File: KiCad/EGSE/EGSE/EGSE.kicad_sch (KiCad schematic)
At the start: 0 parts

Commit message: Kicad is my hell
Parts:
- added MOSFET1, MOSFET2: SIS412DN-T1-GE3, POWERPAK_1212-8, symbol 2025-09-18_19-47-42:SIS412DN-T1-GE3
- added MOSFET3, MOSFET4: SI7617DN-T1-GE3, POWERPAK_1212-8_VIS, symbol 2025-09-18_19-46-24:SI7617DN-T1-GE3
- added U1: BQ24610, Package_DFN_QFN:VQFN-24-1EP_4x4mm_P0.5mm_EP2.45x2.45mm, symbol Battery_Management:BQ24610
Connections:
- new net: MOSFET3.1 (S), MOSFET3.2 (S), MOSFET3.3 (S)
- new net: MOSFET3.5 (D), MOSFET3.6 (D), MOSFET3.7 (D), MOSFET3.8 (D)
- new net: MOSFET1.1 (S), MOSFET1.2 (S), MOSFET1.3 (S), MOSFET2.5 (D), MOSFET2.6 (D), MOSFET2.7 (D), MOSFET2.8 (D), U1.20 (PH)
- new net: MOSFET1.4 (G), U1.21 (HIDRV)
- new net: MOSFET1.5 (D), MOSFET1.6 (D), MOSFET1.7 (D), MOSFET1.8 (D)
- new net: MOSFET2.4 (G), U1.19 (LODRV)
- new net: MOSFET4.1 (S), MOSFET4.2 (S), MOSFET4.3 (S)
- new net: MOSFET4.5 (D), MOSFET4.6 (D), MOSFET4.7 (D), MOSFET4.8 (D)
- new net GND: MOSFET2.1 (S), MOSFET2.2 (S), MOSFET2.3 (S), U1.17 (GND), U1.25 (GND)

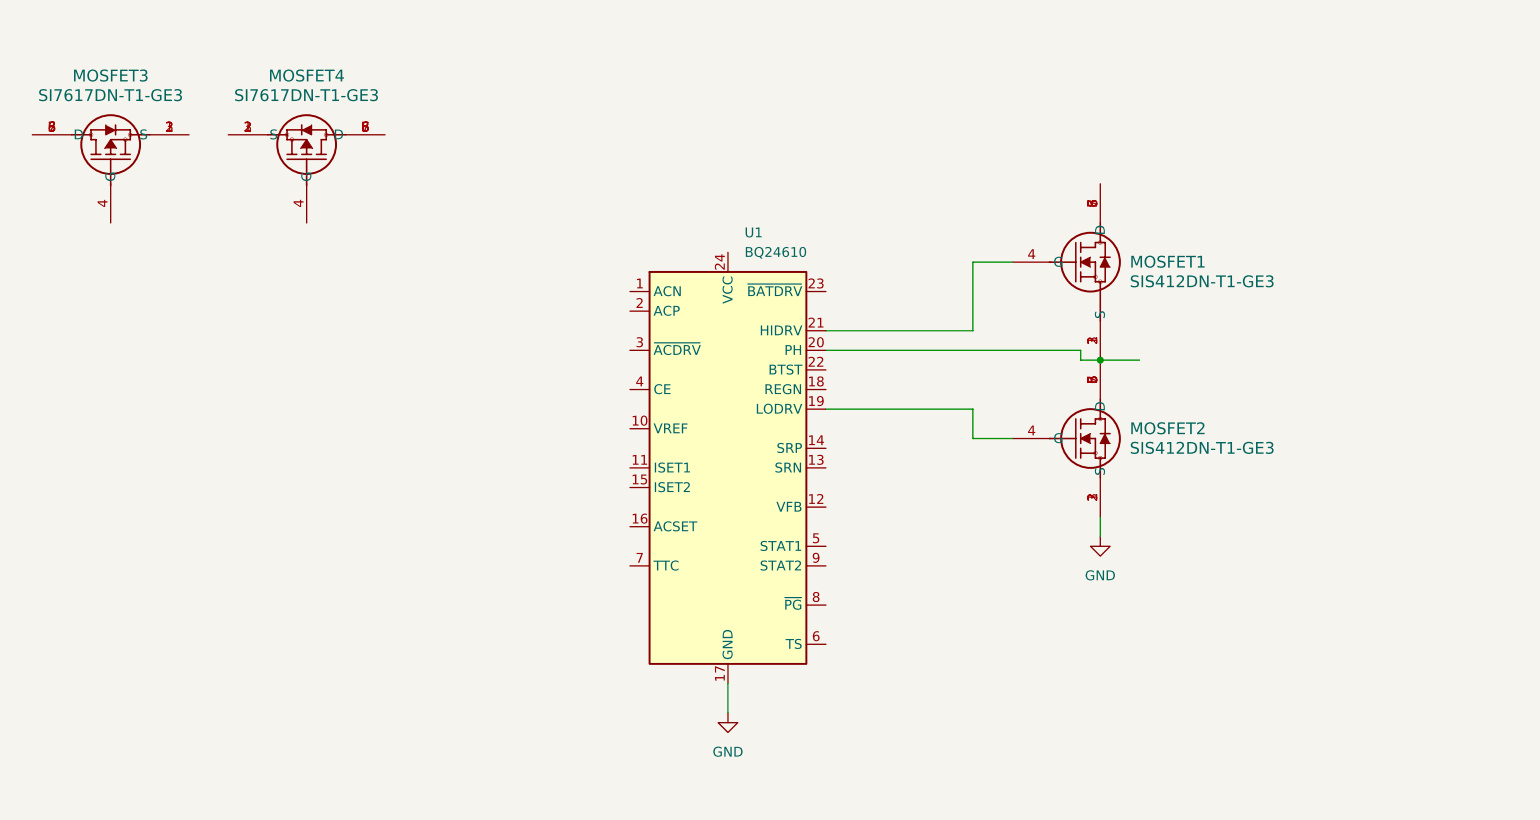
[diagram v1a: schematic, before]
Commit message: Battery Charge Schematic Done
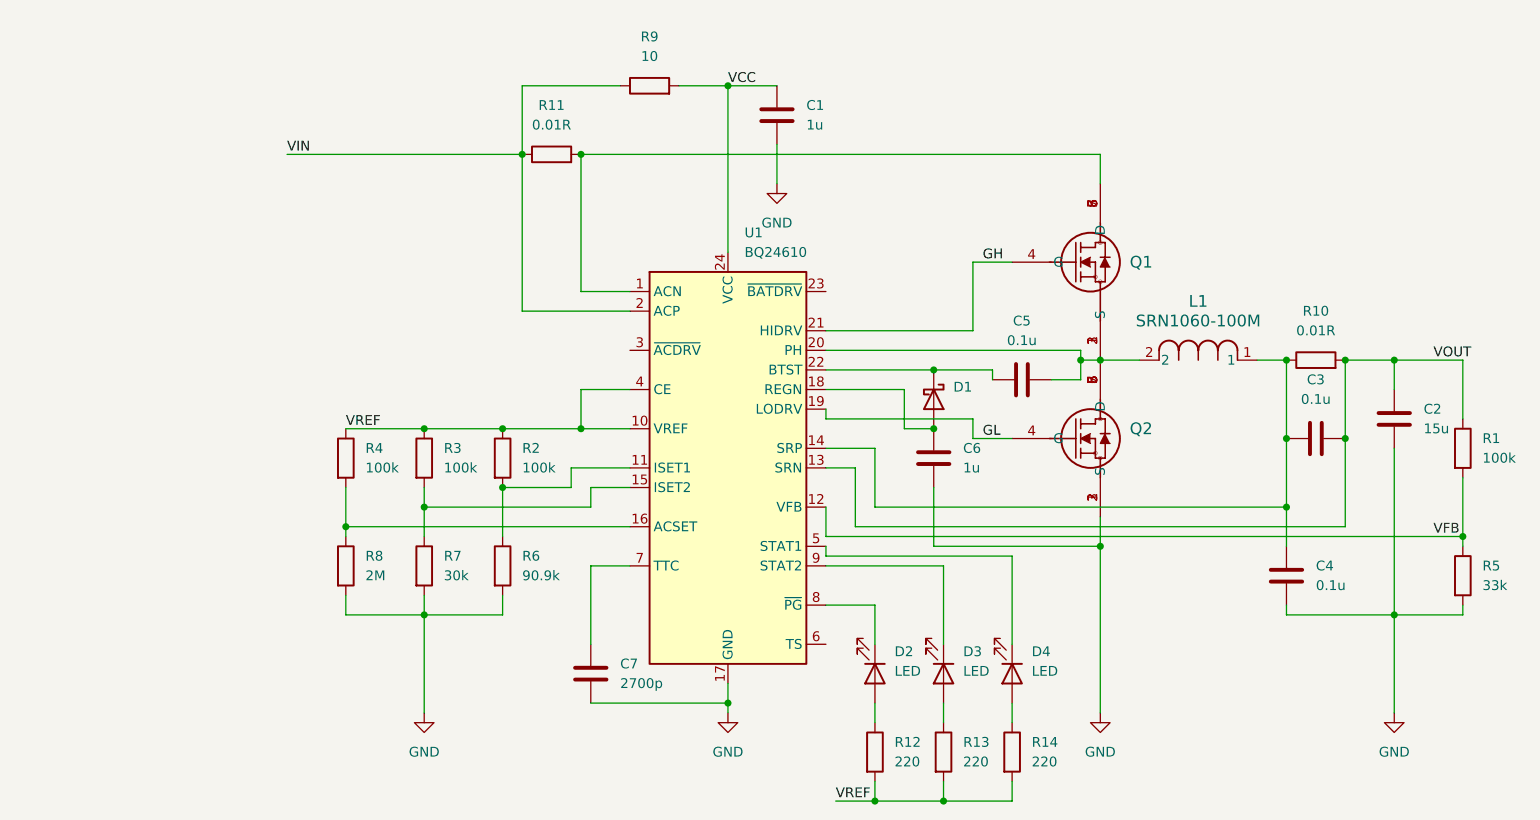
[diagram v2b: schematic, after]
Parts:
- removed MOSFET3, MOSFET4: SI7617DN-T1-GE3, POWERPAK_1212-8_VIS, symbol 2025-09-18_19-46-24:SI7617DN-T1-GE3
- added C1, C6: 1u, Capacitor_SMD:C_0805_2012Metric, symbol Device:C
- added C2: 15u, Capacitor_SMD:C_0805_2012Metric, symbol Device:C
- added C3, C4, C5: 0.1u, Capacitor_SMD:C_0805_2012Metric, symbol Device:C
- added C7: 2700p, Capacitor_SMD:C_0805_2012Metric, symbol Device:C
- added D1: D_Schottky, Diode_SMD:D_SOD-123, symbol Device:D_Schottky
- added D2, D3, D4: LED, symbol Device:LED
- added L1: SRN1060-100M, IND_BOURNS_SRN1060, symbol SRN1060-100M:SRN1060-100M
- added R1, R2, R3, R4: 100k, Resistor_SMD:R_0805_2012Metric, symbol Device:R
- added R10, R11: 0.01R, Resistor_SMD:R_0805_2012Metric, symbol Device:R
- added R12, R13, R14: 220, Resistor_SMD:R_0805_2012Metric, symbol Device:R
- added R5: 33k, Resistor_SMD:R_0805_2012Metric, symbol Device:R
- added R6: 90.9k, Resistor_SMD:R_0805_2012Metric, symbol Device:R
- added R7: 30k, Resistor_SMD:R_0805_2012Metric, symbol Device:R
- added R8: 2M, Resistor_SMD:R_0805_2012Metric, symbol Device:R
- added R9: 10, Resistor_SMD:R_0805_2012Metric, symbol Device:R
- renumbered MOSFET1 to Q1, MOSFET2 to Q2
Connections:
- net GND: now also C1.2, C2.2, C4.1, C6.2, C7.2, R5.2, R6.2, R7.2, R8.2
- net at Q1.1 (S), Q1.2 (S), Q1.3 (S)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: now also C5.2, L1.2
- net GH: now reaches Q1.4 (G), U1.21 (HIDRV)
- net at Q1.5 (D), Q1.6 (D), Q1.7 (D)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: now also U1.1 (ACN), R11.2
- net VREF: now reaches U1.10 (VREF)
- net VREF: now also U1.4 (CE), R12.2, R13.2, R14.2, R2.1, R3.1, R4.1
- net at U1.11 (ISET1): now also R2.2, R6.1
- net VFB: now reaches U1.12 (VFB)
- net VFB: now also R1.2, R5.1
- net VOUT: now reaches U1.13 (SRN)
- net VOUT: now also C2.1, C3.2, R1.1, R10.2
- net at U1.14 (SRP): now also C3.1, C4.2, L1.1, R10.1
- net at U1.15 (ISET2): now also R3.2, R7.1
- net at U1.16 (ACSET): now also R4.2, R8.1
- net at U1.18 (REGN): now also C6.1, D1.2 (A)
- net GL: now reaches Q2.4 (G), U1.19 (LODRV)
- net VIN: now reaches U1.2 (ACP)
- net VIN: now also R11.1, R9.1
- net at U1.22 (BTST): now also C5.1, D1.1 (K)
- net VCC: now reaches U1.24 (VCC)
- net VCC: now also C1.1, R9.2
- net at U1.5 (STAT1): now also D4.1 (K)
- net at U1.7 (TTC): now also C7.1
- net at U1.8 (~{PG}): now also D2.1 (K)
- net at U1.9 (STAT2): now also D3.1 (K)
- new net: D4.2 (A), R14.1
- new net: D3.2 (A), R13.1
- new net: D2.2 (A), R12.1

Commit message: Okay KICAD isn't so bad
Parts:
- removed C1, C6: 1u, Capacitor_SMD:C_0805_2012Metric, symbol Device:C
- removed C2: 15u, Capacitor_SMD:C_0805_2012Metric, symbol Device:C
- removed C3, C4, C5: 0.1u, Capacitor_SMD:C_0805_2012Metric, symbol Device:C
- removed C7: 2700p, Capacitor_SMD:C_0805_2012Metric, symbol Device:C
- removed D1: D_Schottky, Diode_SMD:D_SOD-123, symbol Device:D_Schottky
- removed D2, D3, D4: LED, symbol Device:LED
- removed L1: SRN1060-100M, IND_BOURNS_SRN1060, symbol SRN1060-100M:SRN1060-100M
- removed Q1, Q2: SIS412DN-T1-GE3, POWERPAK_1212-8, symbol 2025-09-18_19-47-42:SIS412DN-T1-GE3
- removed R1, R2, R3, R4: 100k, Resistor_SMD:R_0805_2012Metric, symbol Device:R
- removed R10, R11: 0.01R, Resistor_SMD:R_0805_2012Metric, symbol Device:R
- removed R12, R13, R14: 220, Resistor_SMD:R_0805_2012Metric, symbol Device:R
- removed R5: 33k, Resistor_SMD:R_0805_2012Metric, symbol Device:R
- removed R6: 90.9k, Resistor_SMD:R_0805_2012Metric, symbol Device:R
- removed R7: 30k, Resistor_SMD:R_0805_2012Metric, symbol Device:R
- removed R8: 2M, Resistor_SMD:R_0805_2012Metric, symbol Device:R
- removed R9: 10, Resistor_SMD:R_0805_2012Metric, symbol Device:R
- removed U1: BQ24610, Package_DFN_QFN:VQFN-24-1EP_4x4mm_P0.5mm_EP2.45x2.45mm, symbol Battery_Management:BQ24610
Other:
- added sheet BattCharge (BattCharge.kicad_sch)
- added sheet CP2102 (CP2102.kicad_sch)
- added sheet IO (untitled.kicad_sch)

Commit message: 2016 Cavs Finals
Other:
- sheet IO: file untitled.kicad_sch -> IO.kicad_sch
- sheet IO ports: added VIN; removed none
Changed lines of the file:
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@@
+	(wire
+		(pts
+			(xy 90.17 76.2) (xy 92.71 76.2)
+		)
+		(stroke
+			(width 0)
+			(type default)
+		)
+	)
 	(wire
 		(pts
@@
 	(wire
 		(pts
+			(xy 92.71 60.96) (xy 90.17 60.96)
+		)
+		(stroke
+			(width 0)
+			(type default)
+		)
+	)
+	(wire
+		(pts
 			(xy 121.92 104.14) (xy 121.92 54.61)
 		)
@@
 		(pts
 			(xy 116.84 59.69) (xy 113.03 59.69)
+		)
+		(stroke
+			(width 0)
+			(type default)
+		)
+	)
+	(wire
+		(pts
+			(xy 90.17 60.96) (xy 90.17 76.2)
 		)
 		(stroke
@@
 			)
 		)
-		(property "Sheetfile" "untitled.kicad_sch"
+		(property "Sheetfile" "IO.kicad_sch"
 			(at 92.71 64.0846 0)
 			(effects
@@
 			(effects
 				(font
+					(size 1.27 1.27)
+				)
+				(justify left)
+			)
+		)
+		(pin "VIN" output
+			(at 92.71 60.96 180)
+			(effects
+				(font
